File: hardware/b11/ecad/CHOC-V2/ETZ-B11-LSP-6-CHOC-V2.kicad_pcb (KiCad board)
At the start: 2 copper layers, 163.9 x 90.2 mm, 339 parts

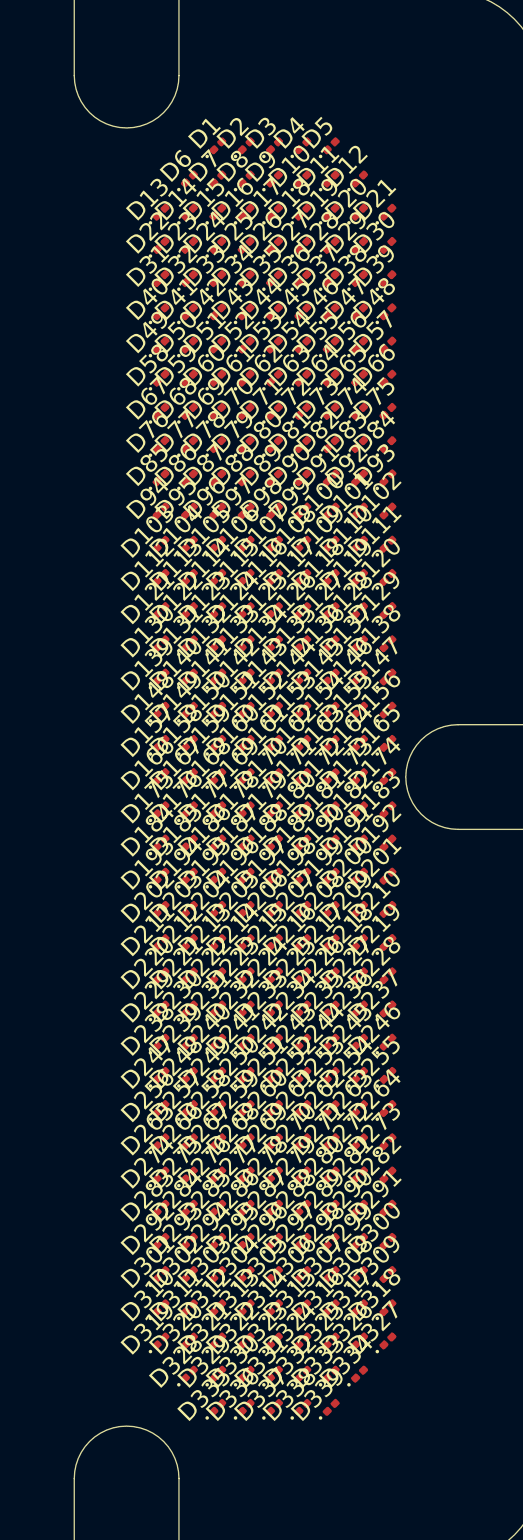
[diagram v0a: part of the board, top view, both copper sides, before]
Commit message: Add B11 display LED placement and stackups
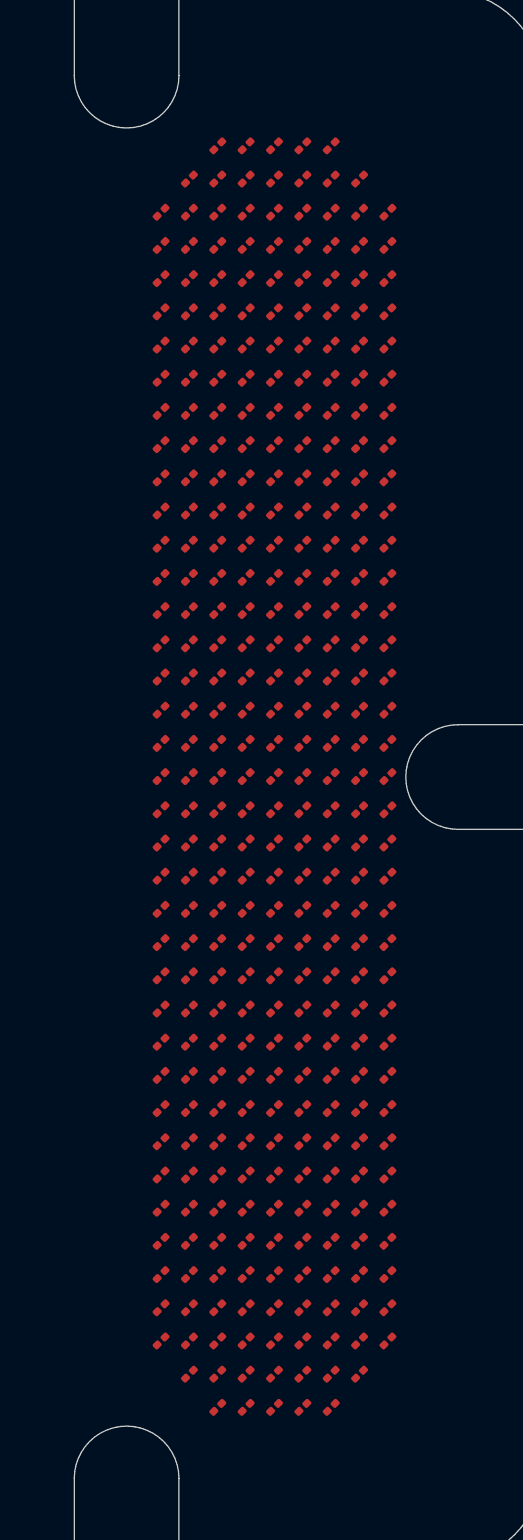
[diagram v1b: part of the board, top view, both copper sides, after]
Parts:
- D1, D10, D100, D101, D102, D103, D104, D105, D106, D107, D108, D109, D11, D110, D111, D112, D113, D114, D115, D116, D117, D118, D119, D12, D120, D121, D122, D123, D124, D125, D126, D127, D128, D129, D13, D130, D131, D132, D133, D134, D135, D136, D137, D138, D139, D14, D140, D141, D142, D143, D144, D145, D146, D147, D148, D149, D15, D150, D151, D152, D153, D154, D155, D156, D157, D158, D159, D16, D160, D161, D162, D163, D164, D165, D166, D167, D168, D169, D17, D170, D171, D172, D173, D174, D175, D176, D177, D178, D179, D18, D180, D181, D182, D183, D184, D185, D186, D187, D188, D189, D19, D190, D191, D192, D193, D194, D195, D196, D197, D198, D199, D2, D20, D200, D201, D202, D203, D204, D205, D206, D207, D208, D209, D21, D210, D211, D212, D213, D214, D215, D216, D217, D218, D219, D22, D220, D221, D222, D223, D224, D225, D226, D227, D228, D229, D23, D230, D231, D232, D233, D234, D235, D236, D237, D238, D239, D24, D240, D241, D242, D243, D244, D245, D246, D247, D248, D249, D25, D250, D251, D252, D253, D254, D255, D256, D257, D258, D259, D26, D260, D261, D262, D263, D264, D265, D266, D267, D268, D269, D27, D270, D271, D272, D273, D274, D275, D276, D277, D278, D279, D28, D280, D281, D282, D283, D284, D285, D286, D287, D288, D289, D29, D290, D291, D292, D293, D294, D295, D296, D297, D298, D299, D3, D30, D300, D301, D302, D303, D304, D305, D306, D307, D308, D309, D31, D310, D311, D312, D313, D314, D315, D316, D317, D318, D319, D32, D320, D321, D322, D323, D324, D325, D326, D327, D328, D329, D33, D330, D331, D332, D333, D334, D335, D336, D337, D338, D339, D34, D35, D36, D37, D38, D39, D4, D40, D41, D42, D43, D44, D45, D46, D47, D48, D49, D5, D50, D51, D52, D53, D54, D55, D56, D57, D58, D59, D6, D60, D61, D62, D63, D64, D65, D66, D67, D68, D69, D7, D70, D71, D72, D73, D74, D75, D76, D77, D78, D79, D8, D80, D81, D82, D83, D84, D85, D86, D87, D88, D89, D9, D90, D91, D92, D93, D94, D95, D96, D97, D98, D99: value LED_0201_0603Metric -> 0201_LED; footprint LED_0201_0603Metric -> 0201_LED
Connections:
- D1 pad 1: (no net) -> LED_CS1
- D1 pad 2: (no net) -> LED_SW3
- D10 pad 1: (no net) -> LED_CS2
- D10 pad 2: (no net) -> LED_SW6
- D100 pad 1: (no net) -> LED_CS12
- D100 pad 2: (no net) -> LED_SW7
- D101 pad 1: (no net) -> LED_CS12
- D101 pad 2: (no net) -> LED_SW8
- D102 pad 1: (no net) -> LED_CS12
- D102 pad 2: (no net) -> LED_SW9
- D103 pad 1: (no net) -> LED_CS13
- D103 pad 2: (no net) -> LED_SW1
- D104 pad 1: (no net) -> LED_CS13
- D104 pad 2: (no net) -> LED_SW2
- D105 pad 1: (no net) -> LED_CS13
- D105 pad 2: (no net) -> LED_SW3
- D106 pad 1: (no net) -> LED_CS13
- D106 pad 2: (no net) -> LED_SW4
- D107 pad 1: (no net) -> LED_CS13
- D107 pad 2: (no net) -> LED_SW5
- D108 pad 1: (no net) -> LED_CS13
- D108 pad 2: (no net) -> LED_SW6
- D109 pad 1: (no net) -> LED_CS13
- D109 pad 2: (no net) -> LED_SW7
- D11 pad 1: (no net) -> LED_CS2
- D11 pad 2: (no net) -> LED_SW7
- D110 pad 1: (no net) -> LED_CS13
- D110 pad 2: (no net) -> LED_SW8
- D111 pad 1: (no net) -> LED_CS13
- D111 pad 2: (no net) -> LED_SW9
- D112 pad 1: (no net) -> LED_CS14
- D112 pad 2: (no net) -> LED_SW1
- D113 pad 1: (no net) -> LED_CS14
- D113 pad 2: (no net) -> LED_SW2
- D114 pad 1: (no net) -> LED_CS14
- D114 pad 2: (no net) -> LED_SW3
- D115 pad 1: (no net) -> LED_CS14
- D115 pad 2: (no net) -> LED_SW4
- D116 pad 1: (no net) -> LED_CS14
- D116 pad 2: (no net) -> LED_SW5
- D117 pad 1: (no net) -> LED_CS14
- D117 pad 2: (no net) -> LED_SW6
- D118 pad 1: (no net) -> LED_CS14
- D118 pad 2: (no net) -> LED_SW7
- D119 pad 1: (no net) -> LED_CS14
- D119 pad 2: (no net) -> LED_SW8
- D12 pad 1: (no net) -> LED_CS2
- D12 pad 2: (no net) -> LED_SW8
- D120 pad 1: (no net) -> LED_CS14
- D120 pad 2: (no net) -> LED_SW9
- D121 pad 1: (no net) -> LED_CS15
- D121 pad 2: (no net) -> LED_SW1
- D122 pad 1: (no net) -> LED_CS15
- D122 pad 2: (no net) -> LED_SW2
- D123 pad 1: (no net) -> LED_CS15
- D123 pad 2: (no net) -> LED_SW3
- D124 pad 1: (no net) -> LED_CS15
- D124 pad 2: (no net) -> LED_SW4
- D125 pad 1: (no net) -> LED_CS15
- D125 pad 2: (no net) -> LED_SW5
- D126 pad 1: (no net) -> LED_CS15
- D126 pad 2: (no net) -> LED_SW6
- D127 pad 1: (no net) -> LED_CS15
- D127 pad 2: (no net) -> LED_SW7
- D128 pad 1: (no net) -> LED_CS15
- D128 pad 2: (no net) -> LED_SW8
- D129 pad 1: (no net) -> LED_CS15
- D129 pad 2: (no net) -> LED_SW9
- D13 pad 1: (no net) -> LED_CS3
- D13 pad 2: (no net) -> LED_SW1
- D130 pad 1: (no net) -> LED_CS16
- D130 pad 2: (no net) -> LED_SW1
- D131 pad 1: (no net) -> LED_CS16
- D131 pad 2: (no net) -> LED_SW2
- D132 pad 1: (no net) -> LED_CS16
- D132 pad 2: (no net) -> LED_SW3
- D133 pad 1: (no net) -> LED_CS16
- D133 pad 2: (no net) -> LED_SW4
- D134 pad 1: (no net) -> LED_CS16
- D134 pad 2: (no net) -> LED_SW5
- D135 pad 1: (no net) -> LED_CS16
- D135 pad 2: (no net) -> LED_SW6
- D136 pad 1: (no net) -> LED_CS16
- D136 pad 2: (no net) -> LED_SW7
- D137 pad 1: (no net) -> LED_CS16
- D137 pad 2: (no net) -> LED_SW8
- D138 pad 1: (no net) -> LED_CS16
- D138 pad 2: (no net) -> LED_SW9
- D139 pad 1: (no net) -> LED_CS17
- D139 pad 2: (no net) -> LED_SW1
- D14 pad 1: (no net) -> LED_CS3
- D14 pad 2: (no net) -> LED_SW2
- D140 pad 1: (no net) -> LED_CS17
- D140 pad 2: (no net) -> LED_SW2
- D141 pad 1: (no net) -> LED_CS17
- D141 pad 2: (no net) -> LED_SW3
- D142 pad 1: (no net) -> LED_CS17
- D142 pad 2: (no net) -> LED_SW4
- D143 pad 1: (no net) -> LED_CS17
- D143 pad 2: (no net) -> LED_SW5
- D144 pad 1: (no net) -> LED_CS17
- D144 pad 2: (no net) -> LED_SW6
- D145 pad 1: (no net) -> LED_CS17
- D145 pad 2: (no net) -> LED_SW7
- D146 pad 1: (no net) -> LED_CS17
- D146 pad 2: (no net) -> LED_SW8
- D147 pad 1: (no net) -> LED_CS17
- D147 pad 2: (no net) -> LED_SW9
- D148 pad 1: (no net) -> LED_CS18
- D148 pad 2: (no net) -> LED_SW1
- D149 pad 1: (no net) -> LED_CS18
- D149 pad 2: (no net) -> LED_SW2
- D15 pad 1: (no net) -> LED_CS3
- D15 pad 2: (no net) -> LED_SW3
- D150 pad 1: (no net) -> LED_CS18
- D150 pad 2: (no net) -> LED_SW3
- D151 pad 1: (no net) -> LED_CS18
- D151 pad 2: (no net) -> LED_SW4
- D152 pad 1: (no net) -> LED_CS18
- D152 pad 2: (no net) -> LED_SW5
- D153 pad 1: (no net) -> LED_CS18
- D153 pad 2: (no net) -> LED_SW6
- D154 pad 1: (no net) -> LED_CS18
- D154 pad 2: (no net) -> LED_SW7
- D155 pad 1: (no net) -> LED_CS18
- D155 pad 2: (no net) -> LED_SW8
- D156 pad 1: (no net) -> LED_CS18
- D156 pad 2: (no net) -> LED_SW9
- D157 pad 1: (no net) -> LED_CS19
- D157 pad 2: (no net) -> LED_SW1
- D158 pad 1: (no net) -> LED_CS19
- D158 pad 2: (no net) -> LED_SW2
- D159 pad 1: (no net) -> LED_CS19
- D159 pad 2: (no net) -> LED_SW3
- D16 pad 1: (no net) -> LED_CS3
- D16 pad 2: (no net) -> LED_SW4
- D160 pad 1: (no net) -> LED_CS19
- D160 pad 2: (no net) -> LED_SW4
- D161 pad 1: (no net) -> LED_CS19
- D161 pad 2: (no net) -> LED_SW5
- D162 pad 1: (no net) -> LED_CS19
- D162 pad 2: (no net) -> LED_SW6
- D163 pad 1: (no net) -> LED_CS19
- D163 pad 2: (no net) -> LED_SW7
- D164 pad 1: (no net) -> LED_CS19
- D164 pad 2: (no net) -> LED_SW8
- D165 pad 1: (no net) -> LED_CS19
- D165 pad 2: (no net) -> LED_SW9
- D166 pad 1: (no net) -> LED_CS20
- D166 pad 2: (no net) -> LED_SW1
- D167 pad 1: (no net) -> LED_CS20
- D167 pad 2: (no net) -> LED_SW2
- D168 pad 1: (no net) -> LED_CS20
- D168 pad 2: (no net) -> LED_SW3
- D169 pad 1: (no net) -> LED_CS20
- D169 pad 2: (no net) -> LED_SW4
- D17 pad 1: (no net) -> LED_CS3
- D17 pad 2: (no net) -> LED_SW5
- D170 pad 1: (no net) -> LED_CS20
- D170 pad 2: (no net) -> LED_SW5
- D171 pad 1: (no net) -> LED_CS20
- D171 pad 2: (no net) -> LED_SW6
- D172 pad 1: (no net) -> LED_CS20
- D172 pad 2: (no net) -> LED_SW7
- D173 pad 1: (no net) -> LED_CS20
- D173 pad 2: (no net) -> LED_SW8
- D174 pad 1: (no net) -> LED_CS20
- D174 pad 2: (no net) -> LED_SW9
- D175 pad 1: (no net) -> LED_CS21
- D175 pad 2: (no net) -> LED_SW1
- D176 pad 1: (no net) -> LED_CS21
- D176 pad 2: (no net) -> LED_SW2
- D177 pad 1: (no net) -> LED_CS21
- D177 pad 2: (no net) -> LED_SW3
- D178 pad 1: (no net) -> LED_CS21
- D178 pad 2: (no net) -> LED_SW4
- D179 pad 1: (no net) -> LED_CS21
- D179 pad 2: (no net) -> LED_SW5
- D18 pad 1: (no net) -> LED_CS3
- D18 pad 2: (no net) -> LED_SW6
- D180 pad 1: (no net) -> LED_CS21
- D180 pad 2: (no net) -> LED_SW6
- D181 pad 1: (no net) -> LED_CS21
- D181 pad 2: (no net) -> LED_SW7
- D182 pad 1: (no net) -> LED_CS21
- D182 pad 2: (no net) -> LED_SW8
- D183 pad 1: (no net) -> LED_CS21
- D183 pad 2: (no net) -> LED_SW9
- D184 pad 1: (no net) -> LED_CS22
- D184 pad 2: (no net) -> LED_SW1
- D185 pad 1: (no net) -> LED_CS22
- D185 pad 2: (no net) -> LED_SW2
- D186 pad 1: (no net) -> LED_CS22
- D186 pad 2: (no net) -> LED_SW3
- D187 pad 1: (no net) -> LED_CS22
- D187 pad 2: (no net) -> LED_SW4
- D188 pad 1: (no net) -> LED_CS22
- D188 pad 2: (no net) -> LED_SW5
- D189 pad 1: (no net) -> LED_CS22
- D189 pad 2: (no net) -> LED_SW6
- D19 pad 1: (no net) -> LED_CS3
- D19 pad 2: (no net) -> LED_SW7
- D190 pad 1: (no net) -> LED_CS22
- D190 pad 2: (no net) -> LED_SW7
- D191 pad 1: (no net) -> LED_CS22
- D191 pad 2: (no net) -> LED_SW8
- D192 pad 1: (no net) -> LED_CS22
- D192 pad 2: (no net) -> LED_SW9
- D193 pad 1: (no net) -> LED_CS23
- D193 pad 2: (no net) -> LED_SW1
- D194 pad 1: (no net) -> LED_CS23
- D194 pad 2: (no net) -> LED_SW2
- D195 pad 1: (no net) -> LED_CS23
- D195 pad 2: (no net) -> LED_SW3
- D196 pad 1: (no net) -> LED_CS23
- D196 pad 2: (no net) -> LED_SW4
- D197 pad 1: (no net) -> LED_CS23
- D197 pad 2: (no net) -> LED_SW5
- D198 pad 1: (no net) -> LED_CS23
- D198 pad 2: (no net) -> LED_SW6
- D199 pad 1: (no net) -> LED_CS23
- D199 pad 2: (no net) -> LED_SW7
- D2 pad 1: (no net) -> LED_CS1
- D2 pad 2: (no net) -> LED_SW4
- D20 pad 1: (no net) -> LED_CS3
- D20 pad 2: (no net) -> LED_SW8
- D200 pad 1: (no net) -> LED_CS23
- D200 pad 2: (no net) -> LED_SW8
- D201 pad 1: (no net) -> LED_CS23
- D201 pad 2: (no net) -> LED_SW9
- D202 pad 1: (no net) -> LED_CS24
- D202 pad 2: (no net) -> LED_SW1
- D203 pad 1: (no net) -> LED_CS24
- D203 pad 2: (no net) -> LED_SW2
- D204 pad 1: (no net) -> LED_CS24
- D204 pad 2: (no net) -> LED_SW3
- D205 pad 1: (no net) -> LED_CS24
- D205 pad 2: (no net) -> LED_SW4
- D206 pad 1: (no net) -> LED_CS24
- D206 pad 2: (no net) -> LED_SW5
- D207 pad 1: (no net) -> LED_CS24
- D207 pad 2: (no net) -> LED_SW6
- D208 pad 1: (no net) -> LED_CS24
- D208 pad 2: (no net) -> LED_SW7
- D209 pad 1: (no net) -> LED_CS24
- D209 pad 2: (no net) -> LED_SW8
- D21 pad 1: (no net) -> LED_CS3
- D21 pad 2: (no net) -> LED_SW9
- D210 pad 1: (no net) -> LED_CS24
- D210 pad 2: (no net) -> LED_SW9
- D211 pad 1: (no net) -> LED_CS25
- D211 pad 2: (no net) -> LED_SW1
- D212 pad 1: (no net) -> LED_CS25
- D212 pad 2: (no net) -> LED_SW2
- D213 pad 1: (no net) -> LED_CS25
- D213 pad 2: (no net) -> LED_SW3
- D214 pad 1: (no net) -> LED_CS25
- D214 pad 2: (no net) -> LED_SW4
- D215 pad 1: (no net) -> LED_CS25
- D215 pad 2: (no net) -> LED_SW5
- D216 pad 1: (no net) -> LED_CS25
- D216 pad 2: (no net) -> LED_SW6
- D217 pad 1: (no net) -> LED_CS25
- D217 pad 2: (no net) -> LED_SW7
- D218 pad 1: (no net) -> LED_CS25
- D218 pad 2: (no net) -> LED_SW8
- D219 pad 1: (no net) -> LED_CS25
- D219 pad 2: (no net) -> LED_SW9
- D22 pad 1: (no net) -> LED_CS4
- D22 pad 2: (no net) -> LED_SW1
- D220 pad 1: (no net) -> LED_CS26
- D220 pad 2: (no net) -> LED_SW1
- D221 pad 1: (no net) -> LED_CS26
- D221 pad 2: (no net) -> LED_SW2
- D222 pad 1: (no net) -> LED_CS26
- D222 pad 2: (no net) -> LED_SW3
- D223 pad 1: (no net) -> LED_CS26
- D223 pad 2: (no net) -> LED_SW4
- D224 pad 1: (no net) -> LED_CS26
- D224 pad 2: (no net) -> LED_SW5
- D225 pad 1: (no net) -> LED_CS26
- D225 pad 2: (no net) -> LED_SW6
- D226 pad 1: (no net) -> LED_CS26
- D226 pad 2: (no net) -> LED_SW7
- D227 pad 1: (no net) -> LED_CS26
- D227 pad 2: (no net) -> LED_SW8
- D228 pad 1: (no net) -> LED_CS26
- D228 pad 2: (no net) -> LED_SW9
- D229 pad 1: (no net) -> LED_CS27
- D229 pad 2: (no net) -> LED_SW1
- D23 pad 1: (no net) -> LED_CS4
- D23 pad 2: (no net) -> LED_SW2
- D230 pad 1: (no net) -> LED_CS27
- D230 pad 2: (no net) -> LED_SW2
- D231 pad 1: (no net) -> LED_CS27
- D231 pad 2: (no net) -> LED_SW3
- D232 pad 1: (no net) -> LED_CS27
- D232 pad 2: (no net) -> LED_SW4
- D233 pad 1: (no net) -> LED_CS27
- D233 pad 2: (no net) -> LED_SW5
- D234 pad 1: (no net) -> LED_CS27
- D234 pad 2: (no net) -> LED_SW6
- D235 pad 1: (no net) -> LED_CS27
- D235 pad 2: (no net) -> LED_SW7
- D236 pad 1: (no net) -> LED_CS27
- D236 pad 2: (no net) -> LED_SW8
- D237 pad 1: (no net) -> LED_CS27
- D237 pad 2: (no net) -> LED_SW9
- D238 pad 1: (no net) -> LED_CS28
- D238 pad 2: (no net) -> LED_SW1
- D239 pad 1: (no net) -> LED_CS28
- D239 pad 2: (no net) -> LED_SW2
- D24 pad 1: (no net) -> LED_CS4
- D24 pad 2: (no net) -> LED_SW3
- D240 pad 1: (no net) -> LED_CS28
- D240 pad 2: (no net) -> LED_SW3
- D241 pad 1: (no net) -> LED_CS28
- D241 pad 2: (no net) -> LED_SW4
- D242 pad 1: (no net) -> LED_CS28
- D242 pad 2: (no net) -> LED_SW5
- D243 pad 1: (no net) -> LED_CS28
- D243 pad 2: (no net) -> LED_SW6
- D244 pad 1: (no net) -> LED_CS28
- D244 pad 2: (no net) -> LED_SW7
- D245 pad 1: (no net) -> LED_CS28
- D245 pad 2: (no net) -> LED_SW8
- D246 pad 1: (no net) -> LED_CS28
- D246 pad 2: (no net) -> LED_SW9
- D247 pad 1: (no net) -> LED_CS29
- D247 pad 2: (no net) -> LED_SW1
- D248 pad 1: (no net) -> LED_CS29
- D248 pad 2: (no net) -> LED_SW2
- D249 pad 1: (no net) -> LED_CS29
- D249 pad 2: (no net) -> LED_SW3
- D25 pad 1: (no net) -> LED_CS4
- D25 pad 2: (no net) -> LED_SW4
- D250 pad 1: (no net) -> LED_CS29
- D250 pad 2: (no net) -> LED_SW4
- D251 pad 1: (no net) -> LED_CS29
- D251 pad 2: (no net) -> LED_SW5
- D252 pad 1: (no net) -> LED_CS29
- D252 pad 2: (no net) -> LED_SW6
- D253 pad 1: (no net) -> LED_CS29
- D253 pad 2: (no net) -> LED_SW7
- D254 pad 1: (no net) -> LED_CS29
- D254 pad 2: (no net) -> LED_SW8
- D255 pad 1: (no net) -> LED_CS29
- D255 pad 2: (no net) -> LED_SW9
- D256 pad 1: (no net) -> LED_CS30
- D256 pad 2: (no net) -> LED_SW1
- D257 pad 1: (no net) -> LED_CS30
- D257 pad 2: (no net) -> LED_SW2
- D258 pad 1: (no net) -> LED_CS30
- D258 pad 2: (no net) -> LED_SW3
- D259 pad 1: (no net) -> LED_CS30
- D259 pad 2: (no net) -> LED_SW4
- D26 pad 1: (no net) -> LED_CS4
- D26 pad 2: (no net) -> LED_SW5
- D260 pad 1: (no net) -> LED_CS30
- D260 pad 2: (no net) -> LED_SW5
- D261 pad 1: (no net) -> LED_CS30
- D261 pad 2: (no net) -> LED_SW6
- D262 pad 1: (no net) -> LED_CS30
- D262 pad 2: (no net) -> LED_SW7
- D263 pad 1: (no net) -> LED_CS30
- D263 pad 2: (no net) -> LED_SW8
- D264 pad 1: (no net) -> LED_CS30
- D264 pad 2: (no net) -> LED_SW9
- D265 pad 1: (no net) -> LED_CS31
- D265 pad 2: (no net) -> LED_SW1
- D266 pad 1: (no net) -> LED_CS31
- D266 pad 2: (no net) -> LED_SW2
- D267 pad 1: (no net) -> LED_CS31
- D267 pad 2: (no net) -> LED_SW3
- D268 pad 1: (no net) -> LED_CS31
- D268 pad 2: (no net) -> LED_SW4
- D269 pad 1: (no net) -> LED_CS31
- D269 pad 2: (no net) -> LED_SW5
- D27 pad 1: (no net) -> LED_CS4
- D27 pad 2: (no net) -> LED_SW6
- D270 pad 1: (no net) -> LED_CS31
- D270 pad 2: (no net) -> LED_SW6
- D271 pad 1: (no net) -> LED_CS31
- D271 pad 2: (no net) -> LED_SW7
- D272 pad 1: (no net) -> LED_CS31
- D272 pad 2: (no net) -> LED_SW8
- D273 pad 1: (no net) -> LED_CS31
- D273 pad 2: (no net) -> LED_SW9
- D274 pad 1: (no net) -> LED_CS32
- D274 pad 2: (no net) -> LED_SW1
- D275 pad 1: (no net) -> LED_CS32
- D275 pad 2: (no net) -> LED_SW2
- D276 pad 1: (no net) -> LED_CS32
- D276 pad 2: (no net) -> LED_SW3
- D277 pad 1: (no net) -> LED_CS32
- D277 pad 2: (no net) -> LED_SW4
- D278 pad 1: (no net) -> LED_CS32
- D278 pad 2: (no net) -> LED_SW5
- D279 pad 1: (no net) -> LED_CS32
- D279 pad 2: (no net) -> LED_SW6
- D28 pad 1: (no net) -> LED_CS4
- D28 pad 2: (no net) -> LED_SW7
- D280 pad 1: (no net) -> LED_CS32
- D280 pad 2: (no net) -> LED_SW7
- D281 pad 1: (no net) -> LED_CS32
- D281 pad 2: (no net) -> LED_SW8
- D282 pad 1: (no net) -> LED_CS32
- D282 pad 2: (no net) -> LED_SW9
- D283 pad 1: (no net) -> LED_CS33
- D283 pad 2: (no net) -> LED_SW1
- D284 pad 1: (no net) -> LED_CS33
- D284 pad 2: (no net) -> LED_SW2
- D285 pad 1: (no net) -> LED_CS33
- D285 pad 2: (no net) -> LED_SW3
- D286 pad 1: (no net) -> LED_CS33
- D286 pad 2: (no net) -> LED_SW4
- D287 pad 1: (no net) -> LED_CS33
- D287 pad 2: (no net) -> LED_SW5
- D288 pad 1: (no net) -> LED_CS33
- D288 pad 2: (no net) -> LED_SW6
- D289 pad 1: (no net) -> LED_CS33
- D289 pad 2: (no net) -> LED_SW7
- D29 pad 1: (no net) -> LED_CS4
- D29 pad 2: (no net) -> LED_SW8
- D290 pad 1: (no net) -> LED_CS33
- D290 pad 2: (no net) -> LED_SW8
- D291 pad 1: (no net) -> LED_CS33
- D291 pad 2: (no net) -> LED_SW9
- D292 pad 1: (no net) -> LED_CS34
- D292 pad 2: (no net) -> LED_SW1
- D293 pad 1: (no net) -> LED_CS34
- D293 pad 2: (no net) -> LED_SW2
- D294 pad 1: (no net) -> LED_CS34
- D294 pad 2: (no net) -> LED_SW3
- D295 pad 1: (no net) -> LED_CS34
- D295 pad 2: (no net) -> LED_SW4
- D296 pad 1: (no net) -> LED_CS34
- D296 pad 2: (no net) -> LED_SW5
- D297 pad 1: (no net) -> LED_CS34
- D297 pad 2: (no net) -> LED_SW6
- D298 pad 1: (no net) -> LED_CS34
- D298 pad 2: (no net) -> LED_SW7
- D299 pad 1: (no net) -> LED_CS34
- D299 pad 2: (no net) -> LED_SW8
- D3 pad 1: (no net) -> LED_CS1
- D3 pad 2: (no net) -> LED_SW5
- D30 pad 1: (no net) -> LED_CS4
- D30 pad 2: (no net) -> LED_SW9
- D300 pad 1: (no net) -> LED_CS34
- D300 pad 2: (no net) -> LED_SW9
- D301 pad 1: (no net) -> LED_CS35
- D301 pad 2: (no net) -> LED_SW1
- D302 pad 1: (no net) -> LED_CS35
- D302 pad 2: (no net) -> LED_SW2
- D303 pad 1: (no net) -> LED_CS35
- D303 pad 2: (no net) -> LED_SW3
- D304 pad 1: (no net) -> LED_CS35
- D304 pad 2: (no net) -> LED_SW4
- D305 pad 1: (no net) -> LED_CS35
- D305 pad 2: (no net) -> LED_SW5
- D306 pad 1: (no net) -> LED_CS35
- D306 pad 2: (no net) -> LED_SW6
- D307 pad 1: (no net) -> LED_CS35
- D307 pad 2: (no net) -> LED_SW7
- D308 pad 1: (no net) -> LED_CS35
- D308 pad 2: (no net) -> LED_SW8
- D309 pad 1: (no net) -> LED_CS35
- D309 pad 2: (no net) -> LED_SW9
- D31 pad 1: (no net) -> LED_CS5
- D31 pad 2: (no net) -> LED_SW1
- D310 pad 1: (no net) -> LED_CS36
- D310 pad 2: (no net) -> LED_SW1
- D311 pad 1: (no net) -> LED_CS36
- D311 pad 2: (no net) -> LED_SW2
- D312 pad 1: (no net) -> LED_CS36
- D312 pad 2: (no net) -> LED_SW3
- D313 pad 1: (no net) -> LED_CS36
- D313 pad 2: (no net) -> LED_SW4
- D314 pad 1: (no net) -> LED_CS36
- D314 pad 2: (no net) -> LED_SW5
- D315 pad 1: (no net) -> LED_CS36
- D315 pad 2: (no net) -> LED_SW6
- D316 pad 1: (no net) -> LED_CS36
- D316 pad 2: (no net) -> LED_SW7
- D317 pad 1: (no net) -> LED_CS36
- D317 pad 2: (no net) -> LED_SW8
- D318 pad 1: (no net) -> LED_CS36
- D318 pad 2: (no net) -> LED_SW9
- D319 pad 1: (no net) -> LED_CS37
- D319 pad 2: (no net) -> LED_SW1
- D32 pad 1: (no net) -> LED_CS5
- D32 pad 2: (no net) -> LED_SW2
- D320 pad 1: (no net) -> LED_CS37
- D320 pad 2: (no net) -> LED_SW2
- D321 pad 1: (no net) -> LED_CS37
- D321 pad 2: (no net) -> LED_SW3
- D322 pad 1: (no net) -> LED_CS37
- D322 pad 2: (no net) -> LED_SW4
- D323 pad 1: (no net) -> LED_CS37
- D323 pad 2: (no net) -> LED_SW5
- D324 pad 1: (no net) -> LED_CS37
- D324 pad 2: (no net) -> LED_SW6
- D325 pad 1: (no net) -> LED_CS37
- D325 pad 2: (no net) -> LED_SW7
- D326 pad 1: (no net) -> LED_CS37
- D326 pad 2: (no net) -> LED_SW8
- D327 pad 1: (no net) -> LED_CS37
- D327 pad 2: (no net) -> LED_SW9
- D328 pad 1: (no net) -> LED_CS38
- D328 pad 2: (no net) -> LED_SW2
- D329 pad 1: (no net) -> LED_CS38
- D329 pad 2: (no net) -> LED_SW3
- D33 pad 1: (no net) -> LED_CS5
- D33 pad 2: (no net) -> LED_SW3
- D330 pad 1: (no net) -> LED_CS38
- D330 pad 2: (no net) -> LED_SW4
- D331 pad 1: (no net) -> LED_CS38
- D331 pad 2: (no net) -> LED_SW5
- D332 pad 1: (no net) -> LED_CS38
- D332 pad 2: (no net) -> LED_SW6
- D333 pad 1: (no net) -> LED_CS38
- D333 pad 2: (no net) -> LED_SW7
- D334 pad 1: (no net) -> LED_CS38
- D334 pad 2: (no net) -> LED_SW8
- D335 pad 1: (no net) -> LED_CS39
- D335 pad 2: (no net) -> LED_SW3
- D336 pad 1: (no net) -> LED_CS39
- D336 pad 2: (no net) -> LED_SW4
- D337 pad 1: (no net) -> LED_CS39
- D337 pad 2: (no net) -> LED_SW5
- D338 pad 1: (no net) -> LED_CS39
- D338 pad 2: (no net) -> LED_SW6
- D339 pad 1: (no net) -> LED_CS39
- D339 pad 2: (no net) -> LED_SW7
- D34 pad 1: (no net) -> LED_CS5
- D34 pad 2: (no net) -> LED_SW4
- D35 pad 1: (no net) -> LED_CS5
- D35 pad 2: (no net) -> LED_SW5
- D36 pad 1: (no net) -> LED_CS5
- D36 pad 2: (no net) -> LED_SW6
- D37 pad 1: (no net) -> LED_CS5
- D37 pad 2: (no net) -> LED_SW7
- D38 pad 1: (no net) -> LED_CS5
- D38 pad 2: (no net) -> LED_SW8
- D39 pad 1: (no net) -> LED_CS5
- D39 pad 2: (no net) -> LED_SW9
- D4 pad 1: (no net) -> LED_CS1
- D4 pad 2: (no net) -> LED_SW6
- D40 pad 1: (no net) -> LED_CS6
- D40 pad 2: (no net) -> LED_SW1
- D41 pad 1: (no net) -> LED_CS6
- D41 pad 2: (no net) -> LED_SW2
- D42 pad 1: (no net) -> LED_CS6
- D42 pad 2: (no net) -> LED_SW3
- D43 pad 1: (no net) -> LED_CS6
- D43 pad 2: (no net) -> LED_SW4
- D44 pad 1: (no net) -> LED_CS6
- D44 pad 2: (no net) -> LED_SW5
- D45 pad 1: (no net) -> LED_CS6
- D45 pad 2: (no net) -> LED_SW6
- D46 pad 1: (no net) -> LED_CS6
- D46 pad 2: (no net) -> LED_SW7
- D47 pad 1: (no net) -> LED_CS6
- D47 pad 2: (no net) -> LED_SW8
- D48 pad 1: (no net) -> LED_CS6
- D48 pad 2: (no net) -> LED_SW9
- D49 pad 1: (no net) -> LED_CS7
- D49 pad 2: (no net) -> LED_SW1
- D5 pad 1: (no net) -> LED_CS1
- D5 pad 2: (no net) -> LED_SW7
- D50 pad 1: (no net) -> LED_CS7
- D50 pad 2: (no net) -> LED_SW2
- D51 pad 1: (no net) -> LED_CS7
- D51 pad 2: (no net) -> LED_SW3
- D52 pad 1: (no net) -> LED_CS7
- D52 pad 2: (no net) -> LED_SW4
- D53 pad 1: (no net) -> LED_CS7
- D53 pad 2: (no net) -> LED_SW5
- D54 pad 1: (no net) -> LED_CS7
- D54 pad 2: (no net) -> LED_SW6
- D55 pad 1: (no net) -> LED_CS7
- D55 pad 2: (no net) -> LED_SW7
- D56 pad 1: (no net) -> LED_CS7
- D56 pad 2: (no net) -> LED_SW8
- D57 pad 1: (no net) -> LED_CS7
- D57 pad 2: (no net) -> LED_SW9
- D58 pad 1: (no net) -> LED_CS8
- D58 pad 2: (no net) -> LED_SW1
- D59 pad 1: (no net) -> LED_CS8
- D59 pad 2: (no net) -> LED_SW2
- D6 pad 1: (no net) -> LED_CS2
- D6 pad 2: (no net) -> LED_SW2
- D60 pad 1: (no net) -> LED_CS8
- D60 pad 2: (no net) -> LED_SW3
- D61 pad 1: (no net) -> LED_CS8
- D61 pad 2: (no net) -> LED_SW4
- D62 pad 1: (no net) -> LED_CS8
- D62 pad 2: (no net) -> LED_SW5
- D63 pad 1: (no net) -> LED_CS8
- D63 pad 2: (no net) -> LED_SW6
- D64 pad 1: (no net) -> LED_CS8
- D64 pad 2: (no net) -> LED_SW7
- D65 pad 1: (no net) -> LED_CS8
- D65 pad 2: (no net) -> LED_SW8
- D66 pad 1: (no net) -> LED_CS8
- D66 pad 2: (no net) -> LED_SW9
- D67 pad 1: (no net) -> LED_CS9
- D67 pad 2: (no net) -> LED_SW1
- D68 pad 1: (no net) -> LED_CS9
- D68 pad 2: (no net) -> LED_SW2
- D69 pad 1: (no net) -> LED_CS9
- D69 pad 2: (no net) -> LED_SW3
- D7 pad 1: (no net) -> LED_CS2
- D7 pad 2: (no net) -> LED_SW3
- D70 pad 1: (no net) -> LED_CS9
- D70 pad 2: (no net) -> LED_SW4
- D71 pad 1: (no net) -> LED_CS9
- D71 pad 2: (no net) -> LED_SW5
- D72 pad 1: (no net) -> LED_CS9
- D72 pad 2: (no net) -> LED_SW6
- D73 pad 1: (no net) -> LED_CS9
- D73 pad 2: (no net) -> LED_SW7
- D74 pad 1: (no net) -> LED_CS9
- D74 pad 2: (no net) -> LED_SW8
- D75 pad 1: (no net) -> LED_CS9
- D75 pad 2: (no net) -> LED_SW9
- D76 pad 1: (no net) -> LED_CS10
- D76 pad 2: (no net) -> LED_SW1
- D77 pad 1: (no net) -> LED_CS10
- D77 pad 2: (no net) -> LED_SW2
- D78 pad 1: (no net) -> LED_CS10
- D78 pad 2: (no net) -> LED_SW3
- D79 pad 1: (no net) -> LED_CS10
- D79 pad 2: (no net) -> LED_SW4
- D8 pad 1: (no net) -> LED_CS2
- D8 pad 2: (no net) -> LED_SW4
- D80 pad 1: (no net) -> LED_CS10
- D80 pad 2: (no net) -> LED_SW5
- D81 pad 1: (no net) -> LED_CS10
- D81 pad 2: (no net) -> LED_SW6
- D82 pad 1: (no net) -> LED_CS10
- D82 pad 2: (no net) -> LED_SW7
- D83 pad 1: (no net) -> LED_CS10
- D83 pad 2: (no net) -> LED_SW8
- D84 pad 1: (no net) -> LED_CS10
- D84 pad 2: (no net) -> LED_SW9
- D85 pad 1: (no net) -> LED_CS11
- D85 pad 2: (no net) -> LED_SW1
- D86 pad 1: (no net) -> LED_CS11
- D86 pad 2: (no net) -> LED_SW2
- D87 pad 1: (no net) -> LED_CS11
- D87 pad 2: (no net) -> LED_SW3
- D88 pad 1: (no net) -> LED_CS11
- D88 pad 2: (no net) -> LED_SW4
- D89 pad 1: (no net) -> LED_CS11
- D89 pad 2: (no net) -> LED_SW5
- D9 pad 1: (no net) -> LED_CS2
- D9 pad 2: (no net) -> LED_SW5
- D90 pad 1: (no net) -> LED_CS11
- D90 pad 2: (no net) -> LED_SW6
- D91 pad 1: (no net) -> LED_CS11
- D91 pad 2: (no net) -> LED_SW7
- D92 pad 1: (no net) -> LED_CS11
- D92 pad 2: (no net) -> LED_SW8
- D93 pad 1: (no net) -> LED_CS11
- D93 pad 2: (no net) -> LED_SW9
- D94 pad 1: (no net) -> LED_CS12
- D94 pad 2: (no net) -> LED_SW1
- D95 pad 1: (no net) -> LED_CS12
- D95 pad 2: (no net) -> LED_SW2
- D96 pad 1: (no net) -> LED_CS12
- D96 pad 2: (no net) -> LED_SW3
- D97 pad 1: (no net) -> LED_CS12
- D97 pad 2: (no net) -> LED_SW4
- D98 pad 1: (no net) -> LED_CS12
- D98 pad 2: (no net) -> LED_SW5
- D99 pad 1: (no net) -> LED_CS12
- D99 pad 2: (no net) -> LED_SW6
